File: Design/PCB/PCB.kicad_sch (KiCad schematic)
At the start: 68 parts, among them J1 KEYSW, J2 12V_BATT, J3 CHARGE, J4 VESC, J5 RGB_LED, J6 BLE_PROG, J7 SWD, J8 CAN, SW1 NRST, U1 UA78M05CKVURG3, U2 TPS62162QDSGRQ1, U3 TPS2116DRLR, U4 MCP111T-195I/LB, U5 STM32F412CGU6, U6 RN4871-I/RM140, U7 TJA1051TK-3, U8 MPU-6050, Y1 NX3225SA-16.000

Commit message: Schematic formatting clean up, added TVS diode to LED PWM
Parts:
- added D10: SC1533-01FTG, Diode_SMD:D_SOD-323, symbol Device:D_TVS
- J2, J3, J4: footprint 2159151002:2159151002 -> Molex_10-84-4020:SHDR2W166P0X635_1X2_1397X762X1397P
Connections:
- net GND: now also D10.1 (A1)
- net PWM: now also D10.2 (A2)
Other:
- note added: "J1 acts as e-stop/charge mode select Connects to external SPDT switch (VBAT = COM)"
- note added: "J1: Molex 50841030 J2, J3, J4: Molex 50841020 Terminals: Molex 366640002"
- note added: "TJA1051 incorporates internal ESD protection for CAN high/low"
- note removed: "J3 acts as e-stop/charge mode select Connects to external SPDT switch (VBAT = COM)"
- note removed: "J4, J5, J6: Molex 50841020 J3: Molex 50841030 Terminals: Molex 366640002"
- moved on the sheet: C20, D9, J5

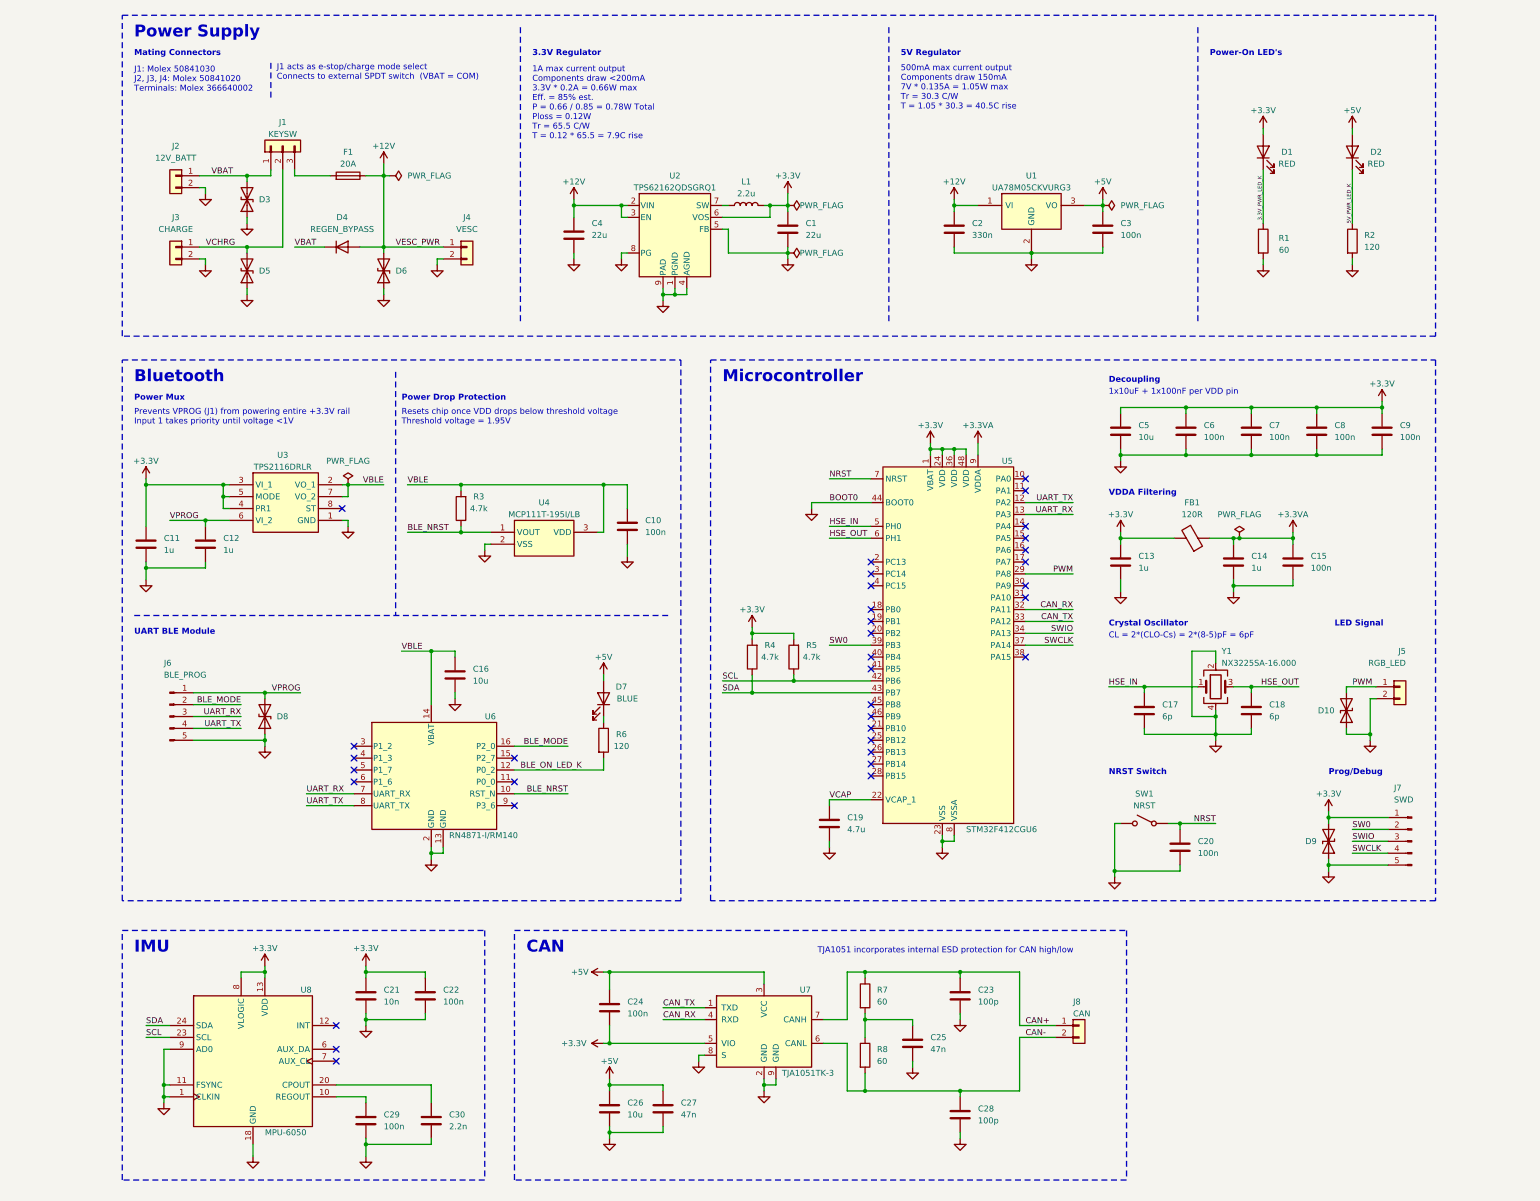
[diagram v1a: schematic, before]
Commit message: Schematic revisions after review
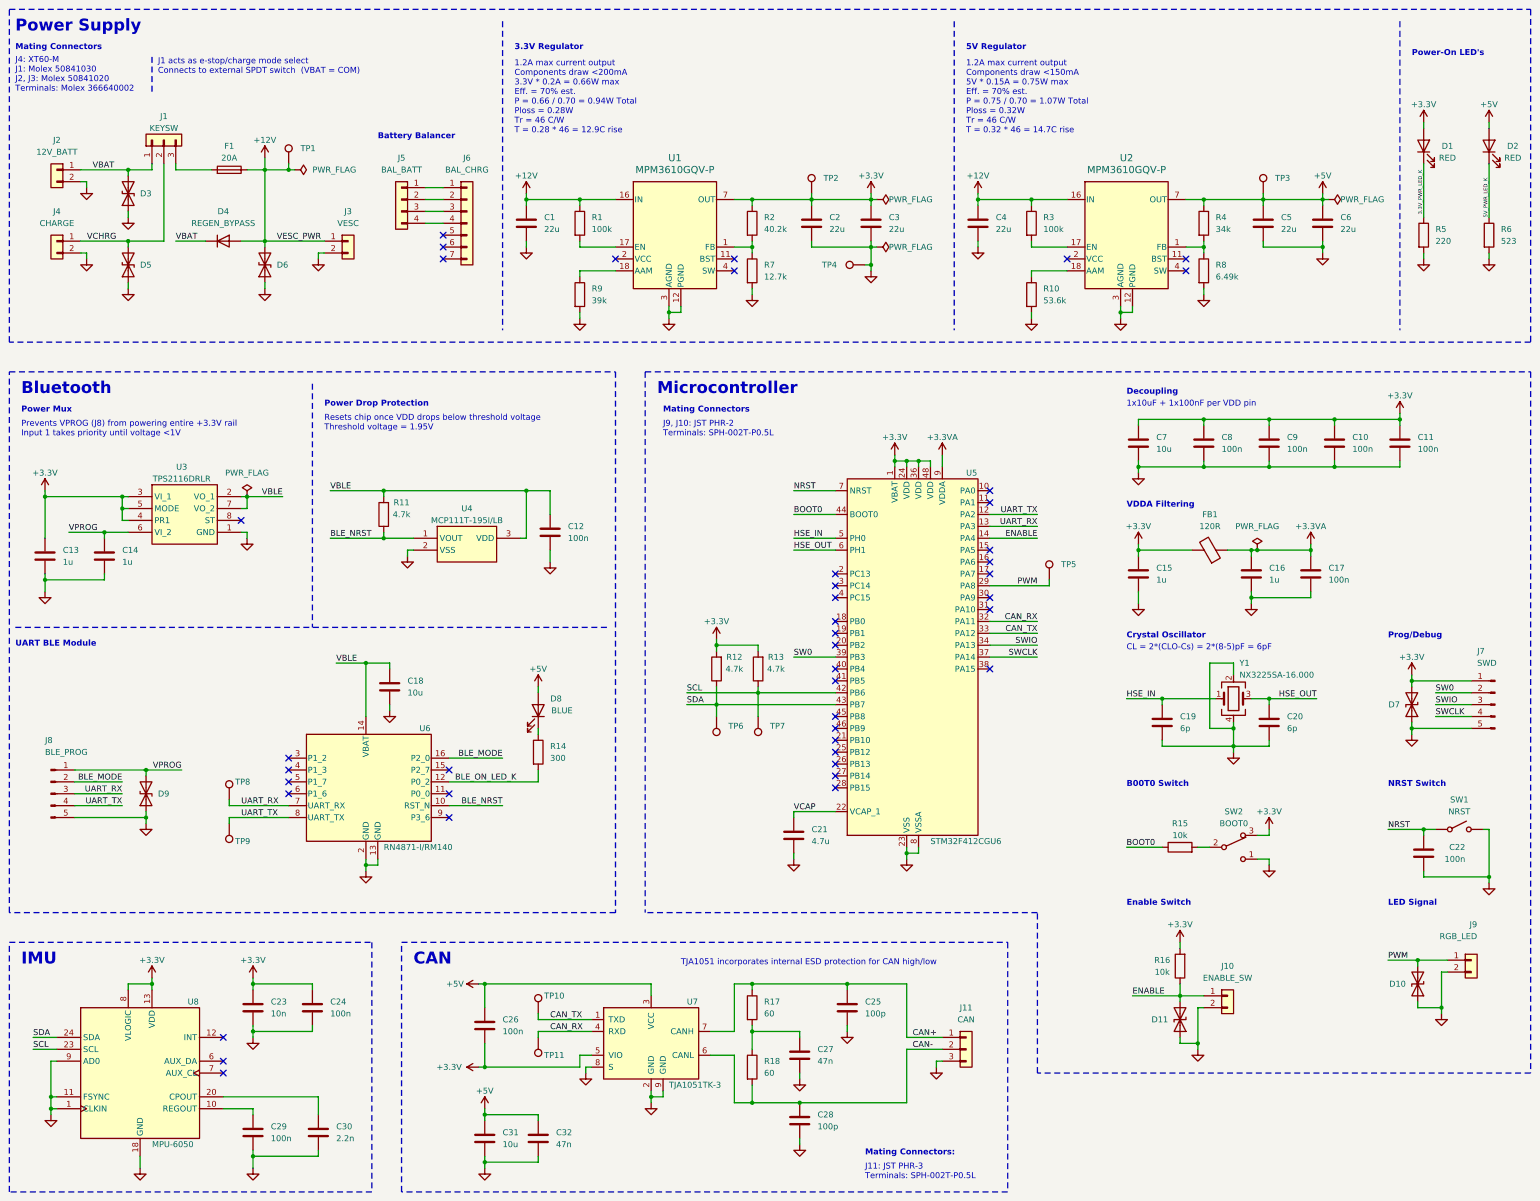
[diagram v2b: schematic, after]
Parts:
- removed D9: SC1533-01FTG, Diode_SMD:D_SOD-323, symbol Device:D_TVS
- removed J8: CAN, symbol Connector_Generic:Conn_01x02
- removed L1: 2.2u, SRP4012CC-2R2M:INDPM4441X120N, symbol SRP4012CC-2R2M:SRP4012CC-2R2M
- removed U1: UA78M05CKVURG3, TPS2116DRLR:SOTFL50P160X60-8N, symbol UA78M05CKVURG3:UA78M05CKVURG3
- removed U2: TPS62162QDSGRQ1, TPS2116DRLR:SOTFL50P160X60-8N, symbol Regulator_Switching:TPS62162DSG
- added C5, C6: 22u, Capacitor_SMD:C_1210_3225Metric, symbol Device:C
- added D11, D7: SC1533-01FTG, Diode_SMD:D_SOD-323, symbol Device:D_TVS
- added J10: ENABLE_SW, Connector_JST:JST_PH_B2B-PH-K_1x02_P2.00mm_Vertical, symbol Connector_Generic:Conn_01x02
- added J11: CAN, Connector_JST:JST_PH_B3B-PH-K_1x03_P2.00mm_Vertical, symbol Connector_Generic:Conn_01x03
- added J5: BAL_BATT, Connector_JST:JST_XH_B4B-XH-A_1x04_P2.50mm_Vertical, symbol Connector_Generic:Conn_01x04
- added J6: BAL_CHRG, Connector_JST:JST_XH_B7B-XH-A_1x07_P2.50mm_Vertical, symbol Connector_Generic:Conn_01x07
- added R10: 53.6k, Resistor_SMD:R_0603_1608Metric, symbol Device:R
- added R14: 300, Resistor_SMD:R_0603_1608Metric, symbol Device:R
- added R15, R16: 10k, Resistor_SMD:R_0603_1608Metric, symbol Device:R
- added R3: 100k, Resistor_SMD:R_0603_1608Metric, symbol Device:R
- added R4: 34k, Resistor_SMD:R_0603_1608Metric, symbol Device:R
- added R5: 220, Resistor_SMD:R_0603_1608Metric, symbol Device:R
- added R7: 12.7k, Resistor_SMD:R_0603_1608Metric, symbol Device:R
- added R8: 6.49k, Resistor_SMD:R_0603_1608Metric, symbol Device:R
- added R9: 39k, Resistor_SMD:R_0603_1608Metric, symbol Device:R
- added SW2: BOOT0, AYZ0102AURLC:AYZ0102AURLC, symbol Switch:SW_SPDT_321
- added TP1, TP10, TP11, TP2, TP3, TP4, TP5, TP6, TP7, TP8, TP9: TestPoint, RCU-0C:RESC1608X50N, symbol Connector:TestPoint
- added U1, U2: MPM3610GQV-P, MPM3610GQV-P:QFN3p0x5p0x1p6_MPM3610_MNP, symbol MPM3610GQV-P:MPM3610GQV-P
- C2: value 330n -> 22u; footprint Capacitor_SMD:C_0603_1608Metric -> Capacitor_SMD:C_1210_3225Metric; PN GCJ188R91E334KA01D -> GRM32ER71E226KE15L
- C3: value 100n -> 22u; footprint Capacitor_SMD:C_0603_1608Metric -> Capacitor_SMD:C_1210_3225Metric; PN GRM188R72A104KA35J -> GRM32ER71E226KE15L
- J4: renamed from J3; footprint Molex_10-84-4020:SHDR2W166P0X635_1X2_1397X762X1397P -> Connector_AMASS:AMASS_XT60-F_1x02_P7.20mm_Vertical; PN 10844020 -> (none)
- J9: renamed from J5; footprint (none) -> Connector_JST:JST_PH_B2B-PH-K_1x02_P2.00mm_Vertical; PN (none) -> B2B-PH-K
- R1: value 60 -> 100k; PN ERJ-UP3F60R4V -> ERJ-UP3F1003V
- R2: value 120 -> 40.2k; PN ERJ-PA3F1200V -> RCS060340K2FKEA
- R6: value 120 -> 523; PN ERJ-PA3F1200V -> ERJ-PA3F5230V
- renumbered C8 to C10, C9 to C11, C10 to C12, C11 to C13, C12 to C14, C13 to C15, C14 to C16, C15 to C17, C16 to C18, C17 to C19, C18 to C20, C19 to C21, C20 to C22, C21 to C23, C22 to C24, C23 to C25, C24 to C26, C25 to C27, C26 to C31, C27 to C32, C5 to C7, C6 to C8, C7 to C9, D7 to D8, D8 to D9, J4 to J3, J6 to J8, R3 to R11, R4 to R12, R5 to R13, R7 to R17, R8 to R18
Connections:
- net +12V: now also C1.1, R1.1, R3.1, TP1.1, U1.16 (IN), U2.16 (IN); no longer C2.1
- net +3.3V: now also C2.1, C3.1, R2.1, D7.2 (A2), R16.2, SW2.3 (A), TP2.1, U1.7 (OUT), U1.8 (OUT), U1.9 (OUT); no longer C1.1
- net +5V: now also C5.1, C6.1, R4.1, TP3.1, U2.7 (OUT), U2.8 (OUT), U2.9 (OUT); no longer C3.1
- net 3.3V_PWR_LED_K: now also R5.1; no longer R1.1
- net 5V_PWR_LED_K: now also R6.1; no longer R2.1
- net BLE_ON_LED_K: now also R14.2; no longer R6.2
- net CAN+: now also J11.1 (Pin_1)
- net CAN-: now also J11.2 (Pin_2)
- net CAN_RX: now also TP11.1
- net CAN_TX: now also TP10.1
- net GND: now also R6.2, C5.2, C6.2, D11.1 (A1), D7.1 (A1), J10.2 (Pin_2), J11.3 (Pin_3), R10.2, R5.2, R7.2, R8.2, R9.2, SW2.1 (C), TP4.1, U1.12 (PGND), U1.13 (PGND), U1.14 (PGND), U1.3 (AGND), U2.12 (PGND), U2.13 (PGND), U2.14 (PGND), U2.3 (AGND); no longer R1.2, R2.2, U5.44 (BOOT0)
- net PWM: now also TP5.1
- net SCL: now also TP7.1
- net SDA: now also TP6.1
- net UART_RX: now also TP8.1
- net UART_TX: now also TP9.1
- net ENABLE: now reaches U5.14 (PA4)
- net ENABLE: now also D11.2 (A2), J10.1 (Pin_1), R16.1
- net at D8.1 (K): now also R14.1; no longer R6.1
- new net: R15.2, SW2.2 (B)
- new net: R4.2, R8.1, U2.1 (FB)
- new net: R9.1, U1.18 (AAM)
- new net: R3.2, U2.17 (EN)
- new net: U2.10 (NC), U2.15 (NC), U2.19 (NC), U2.20 (NC)
- new net: R10.1, U2.18 (AAM)
- new net: U2.4 (SW), U2.5 (SW), U2.6 (SW)
- new net: R2.2, R7.1, U1.1 (FB)
- new net: U1.10 (NC), U1.15 (NC), U1.19 (NC), U1.20 (NC)
- new net: R1.2, U1.17 (EN)
- new net: U1.4 (SW), U1.5 (SW), U1.6 (SW)
- new net: J5.1 (Pin_1), J6.1 (Pin_1)
- new net: J5.2 (Pin_2), J6.2 (Pin_2)
- new net: J5.3 (Pin_3), J6.3 (Pin_3)
- new net: J5.4 (Pin_4), J6.4 (Pin_4)
- new net BOOT0: R15.1, U5.44 (BOOT0)
- no-connect marks 35 -> 43
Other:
- note added: "1.2A max current output Components draw <150mA 5V * 0.15A = 0.75W max Eff. = 70% est. P = 0.75 / 0.70 = 1.07W Total Ploss = 0.32W Tr = 46 C/W T = 0.32 * 46 = 14.7C rise"
- note added: "1.2A max current output Components draw <200mA 3.3V * 0.2A = 0.66W max Eff. = 70% est. P = 0.66 / 0.70 = 0.94W Total Ploss = 0.28W Tr = 46 C/W T = 0.28 * 46 = 12.9C rise"
- note added: "B00T0 Switch"
- note added: "Battery Balancer"
- note added: "Enable Switch"
- note added: "J11: JST PHR-3 Terminals: SPH-002T-P0.5L"
- note added: "J4: XT60-M J1: Molex 50841030 J2, J3: Molex 50841020 Terminals: Molex 366640002"
- note added: "J9, J10: JST PHR-2 Terminals: SPH-002T-P0.5L"
- note added: "Mating Connectors:"
- note added: "Prevents VPROG (J8) from powering entire +3.3V rail Input 1 takes priority until voltage <1V"
- note removed: "1A max current output Components draw <200mA 3.3V * 0.2A = 0.66W max Eff. = 85% est. P = 0.66 / 0.85 = 0.78W Total Ploss = 0.12W Tr = 65.5 C/W T = 0.12 * 65.5 = 7.9C rise"
- note removed: "500mA max current output Components draw 150mA 7V * 0.135A = 1.05W max Tr = 30.3 C/W T = 1.05 * 30.3 = 40.5C rise"
- note removed: "J1: Molex 50841030 J2, J3, J4: Molex 50841020 Terminals: Molex 366640002"
- note removed: "Prevents VPROG (J1) from powering entire +3.3V rail Input 1 takes priority until voltage <1V"
- moved on the sheet: C10, C11, C12, C13, C14, C15, C16, C17, C18, C19, C20, C21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

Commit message: First pass at PCB layout and routing
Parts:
- removed J1: KEYSW, Molex_10-84-4030:SHDR3W166P0X635_1X3_2032X762X1422P, symbol Connector_Generic:Conn_01x03
- removed J2: 12V_BATT, Molex_10-84-4020:SHDR2W166P0X635_1X2_1397X762X1397P, symbol Connector_Generic:Conn_01x02
- removed J3: VESC, Molex_10-84-4020:SHDR2W166P0X635_1X2_1397X762X1397P, symbol Connector_Generic:Conn_01x02
- removed TP5, TP8, TP9: TestPoint, RCU-0C:RESC1608X50N, symbol Connector:TestPoint
- added D12: NUP2105L, Package_TO_SOT_SMD:SOT-23, symbol Power_Protection:NUP2105L
- added H1, H2, H3: MountingHole_Pad, MountingHole:MountingHole_3.2mm_M3_DIN965_Pad, symbol Mechanical:MountingHole_Pad
- added J1: COM_SW, MountingHole:MountingHole_2.7mm_Pad, symbol Connector:Conn_01x01_Pin
- added J10: VESC-, MountingHole:MountingHole_2.7mm_Pad, symbol Connector:Conn_01x01_Pin
- added J2: CHRG_SW, MountingHole:MountingHole_2.7mm_Pad, symbol Connector:Conn_01x01_Pin
- added J3: LOAD_SW, MountingHole:MountingHole_2.7mm_Pad, symbol Connector:Conn_01x01_Pin
- added J4: BATT+, MountingHole:MountingHole_2.7mm_Pad, symbol Connector:Conn_01x01_Pin
- added J5: BATT-, MountingHole:MountingHole_2.7mm_Pad, symbol Connector:Conn_01x01_Pin
- added J9: VESC+, MountingHole:MountingHole_2.7mm_Pad, symbol Connector:Conn_01x01_Pin
- J12: renamed from J8; value BLE_PROG -> BLE PROG
- J14: renamed from J10; value ENABLE_SW -> ENABLE
- T1: renamed from TP1; footprint RCU-0C:RESC1608X50N -> RCU-0C:TP+195X110
- T10: renamed from TP10; footprint RCU-0C:RESC1608X50N -> RCU-0C:TP+195X110
- T11: renamed from TP11; footprint RCU-0C:RESC1608X50N -> RCU-0C:TP+195X110
- T2: renamed from TP2; footprint RCU-0C:RESC1608X50N -> RCU-0C:TP+195X110
- T3: renamed from TP3; footprint RCU-0C:RESC1608X50N -> RCU-0C:TP+195X110
- T4: renamed from TP4; footprint RCU-0C:RESC1608X50N -> RCU-0C:TP+195X110
- T6: renamed from TP6; footprint RCU-0C:RESC1608X50N -> RCU-0C:TP+195X110
- T7: renamed from TP7; footprint RCU-0C:RESC1608X50N -> RCU-0C:TP+195X110
- renumbered J7 to J11, J9 to J13, J11 to J15, J5 to J6, J6 to J7, J4 to J8
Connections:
- net +12V: now also D4.1 (A), J9.1 (Pin_1); no longer D4.2 (A)
- net BLE_MODE: now also J12.4 (Pin_4); no longer J12.2 (Pin_2)
- net CAN+: now also J15.2 (Pin_2), D12.2 (K); no longer J15.1 (Pin_1)
- net CAN-: now also J15.1 (Pin_1), D12.1 (K); no longer J15.2 (Pin_2)
- net GND: now also D12.3 (A), H1.1, H2.1, H3.1, J10.1 (Pin_1), J5.1 (Pin_1)
- net SW0: now also J11.4 (Pin_4); no longer J11.2 (Pin_2)
- net SWCLK: now also J11.3 (Pin_3); no longer J11.4 (Pin_4)
- net SWIO: now also J11.2 (Pin_2); no longer J11.3 (Pin_3)
- net UART_RX: now also J12.2 (Pin_2); no longer J12.3 (Pin_3)
- net UART_TX: now also J12.3 (Pin_3); no longer J12.4 (Pin_4)
- net VBAT: now also D4.2 (K), J1.1 (Pin_1), J4.1 (Pin_1); no longer D4.1 (K)
- net VCHRG: now also J2.1 (Pin_1)
- net 12V_FUSE: now reaches F1.3, F1.4
- net 12V_FUSE: now also J3.1 (Pin_1)
- net 5V_FB: now reaches R4.2, R8.1, U2.1 (FB)
- net 3.3V_FB: now reaches R2.2, R7.1, U1.1 (FB)
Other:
- note added: "J1-J3 act as e-stop/charge mode select Connect to external SPDT switch (VBAT = COM)"
- note added: "J8: XT60-M"
- note added: "M3 Mounting Holes"
- note removed: "J1 acts as e-stop/charge mode select Connects to external SPDT switch (VBAT = COM)"
- note removed: "J4: XT60-M J1: Molex 50841030 J2, J3: Molex 50841020 Terminals: Molex 366640002"
- note removed: "TJA1051 incorporates internal ESD protection for CAN high/low"
- moved on the sheet: C2, C25, C26, C27, C28, C3, C31, C32, D3, D5, D6, F1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

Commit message: Added final pcb design and manufacturing files
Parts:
- D3: MPN (none) -> PJGBLC12CR100001; Manufactuer (none) -> Panjit; PN PJGBLC12CR100001 -> (none)
- D4: MPN (none) -> SBM3060VDC-AU_R2_006A1; Manufacturer (none) -> Panjit; Manufacturer_Name PANJIT International Inc -> (none); Manufacturer_Part_Number SBM3060VDC-AU_R2_006A1 -> (none)
- D5, D6: MPN (none) -> PJGBLC12CR100001; Manufacturer (none) -> Panjit; PN PJGBLC12CR100001 -> (none)
- F1: MPN (none) -> 3568; Manufacturer (none) -> Keystone Electronics; Manufacturer_Name Keystone Electronics -> (none); Manufacturer_Part_Number 3568 -> (none)
- J6: MPN (none) -> B4B-XH-A; Manufacturer (none) -> JST
- J7: Manufacturer (none) -> B7B-XH-A
- J8: MPN (none) -> XT60-F; Manufacturer (none) -> AMASS
- T1: MPN (none) -> RCU-0C; Manufacturer (none) -> TE Connectivity; PN RCU-0C -> (none)
- U1, U2: MPN (none) -> MPM3610GQV-P
- U6: MPN (none) -> RN4871-I/RM140
- U8: MPN (none) -> MPU-6050
